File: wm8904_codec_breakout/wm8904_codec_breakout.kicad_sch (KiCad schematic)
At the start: 5 parts, among them J101 Conn_01x12_Female, J102 Conn_01x12_Female, J103 AudioJack3, J104 AudioJack3, U101 AMS1117-1.8

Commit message: WIP
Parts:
- added TP101: 1V8, TestPoint:TestPoint_Pad_D1.5mm, symbol Connector:TestPoint
- added TP102: GND, TestPoint:TestPoint_Pad_D1.5mm, symbol Connector:TestPoint
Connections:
- net 1V8: now also TP101.1
- net GND: now also TP102.1
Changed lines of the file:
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@@
+    )
+  )
+  (global_label "1V8" (shape input) (at 205.74 52.07 270) (fields_autoplaced)
+    (effects (font (size 1.27 1.27)) (justify right))
+    (property "Intersheet References" "${INTERSHEET_REFS}" (id 0) (at 205.8194 57.9907 90)
+      (effects (font (size 1.27 1.27)) (justify right) hide)
     )
   )
@@
     (pin "T")
   )
+  (symbol (lib_id "power:GND") (at 205.74 35.56 0) (unit 1)
+    (in_bom yes) (on_board yes) (fields_autoplaced)
+    (property "Reference" "#PWR0123" (id 0) (at 205.74 41.91 0)
+      (effects (font (size 1.27 1.27)) hide)
+    )
+    (property "Value" "GND" (id 1) (at 205.74 40.64 0))
+    (property "Footprint" "" (id 2) (at 205.74 35.56 0)
+      (effects (font (size 1.27 1.27)) hide)
+    )
+    (property "Datasheet" "" (id 3) (at 205.74 35.56 0)
+      (effects (font (size 1.27 1.27)) hide)
+    )
+    (pin "1")
+  )
   (symbol (lib_id "Connector:Conn_01x12_Female") (at 121.92 83.82 0) (unit 1)
     (in_bom yes) (on_board yes) (fields_autoplaced)
@@
     (pin "1")
   )
+  (symbol (lib_id "Connector:TestPoint") (at 205.74 52.07 0) (unit 1)
+    (in_bom yes) (on_board yes) (fields_autoplaced)
+    (property "Reference" "TP101" (id 0) (at 208.28 47.4979 0)
+      (effects (font (size 1.27 1.27)) (justify left))
+    )
+    (property "Value" "1V8" (id 1) (at 208.28 50.0379 0)
+      (effects (font (size 1.27 1.27)) (justify left))
+    )
+    (property "Footprint" "TestPoint:TestPoint_Pad_D1.5mm" (id 2) (at 210.82 52.07 0))
+    (property "Datasheet" "~" (id 3) (at 210.82 52.07 0)
+      (effects (font (size 1.27 1.27)) hide)
+    )
+    (property "JLCPCB BOM" "False" (id 4) (at 205.74 52.07 0)
+      (effects (font (size 1.27 1.27)) hide)
+    )
+    (pin "1")
+  )
   (symbol (lib_id "power:GND") (at 114.3 138.43 0) (unit 1)
     (in_bom yes) (on_board yes) (fields_autoplaced)
@@
     (pin "2")
     (pin "3")
+  )
+  (symbol (lib_id "Connector:TestPoint") (at 205.74 35.56 0) (unit 1)
+    (in_bom yes) (on_board yes) (fields_autoplaced)
+    (property "Reference" "TP102" (id 0) (at 208.28 30.9879 0)
+      (effects (font (size 1.27 1.27)) (justify left))
+    )
+    (property "Value" "GND" (id 1) (at 208.28 33.5279 0)
+      (effects (font (size 1.27 1.27)) (justify left))
+    )
+    (property "Footprint" "TestPoint:TestPoint_Pad_D1.5mm" (id 2) (at 210.82 35.56 0))
+    (property "Datasheet" "~" (id 3) (at 210.82 35.56 0)
+      (effects (font (size 1.27 1.27)) hide)
+    )
+    (property "JLCPCB BOM" "False" (id 4) (at 205.74 35.56 0)
+      (effects (font (size 1.27 1.27)) hide)
+    )
+    (pin "1")
   )
   (sheet (at 180.34 69.85) (size 30.48 74.93) (fields_autoplaced)
@@
       (reference "#PWR0122") (unit 1) (value "GND") (footprint "")
     )
+    (path "/43064d00-084c-4e4c-8e6c-67264db5fdd4"
+      (reference "#PWR0123") (unit 1) (value "GND") (footprint "")
+    )
     (path "/7803a0ea-b6d3-457b-b195-42c8dc80b579/b0748b99-67ee-4e5a-be57-fcef590b69aa"
       (reference "C201") (unit 1) (value "0.1u") (footprint "Capacitor_SMD:C_0402_1005Metric")
@@
       (reference "R206") (unit 1) (value "20R") (footprint "Resistor_SMD:R_0603_1608Metric")
     )
+    (path "/6f172490-e7c3-45a0-aafa-f94d5c12df3c"
+      (reference "TP101") (unit 1) (value "1V8") (footprint "TestPoint:TestPoint_Pad_D1.5mm")
+    )
+    (path "/ae81fe48-d57e-4488-a23e-f57c11561913"
+      (reference "TP102") (unit 1) (value "GND") (footprint "TestPoint:TestPoint_Pad_D1.5mm")
+    )
     (path "/952e9d28-22f9-43e0-bee5-7380cf9b61ad"

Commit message: final touches + v1 jlcpcb fab files
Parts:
- removed TP101: 1V8, TestPoint:TestPoint_Pad_D1.5mm, symbol Connector:TestPoint
- removed TP102: GND, TestPoint:TestPoint_Pad_D1.5mm, symbol Connector:TestPoint
- J103, J104: LCSC Part (none) -> C707224; MSCS Part C707224 -> (none)
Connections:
- net 1V8: now also J101.12 (Pin_12)
- net VDD: no longer J101.12 (Pin_12)
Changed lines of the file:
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@@
-    )
-  )
-  (global_label "VDD" (shape input) (at 116.84 99.06 180) (fields_autoplaced)
-    (effects (font (size 1.27 1.27)) (justify right))
-    (property "Intersheet References" "${INTERSHEET_REFS}" (id 0) (at 110.7983 98.9806 0)
-      (effects (font (size 1.27 1.27)) (justify right) hide)
     )
   )
@@
     )
   )
-  (global_label "1V8" (shape input) (at 205.74 52.07 270) (fields_autoplaced)
-    (effects (font (size 1.27 1.27)) (justify right))
-    (property "Intersheet References" "${INTERSHEET_REFS}" (id 0) (at 205.8194 57.9907 90)
-      (effects (font (size 1.27 1.27)) (justify right) hide)
-    )
-  )
   (global_label "LINEOUTFB" (shape input) (at 180.34 87.63 180) (fields_autoplaced)
     (effects (font (size 1.27 1.27)) (justify right))
@@
     (effects (font (size 1.27 1.27)) (justify right))
     (property "Intersheet References" "${INTERSHEET_REFS}" (id 0) (at 107.4721 91.3606 0)
+      (effects (font (size 1.27 1.27)) (justify right) hide)
+    )
+  )
+  (global_label "1V8" (shape input) (at 116.84 99.06 180) (fields_autoplaced)
+    (effects (font (size 1.27 1.27)) (justify right))
+    (property "Intersheet References" "${INTERSHEET_REFS}" (id 0) (at 110.9193 99.1394 0)
       (effects (font (size 1.27 1.27)) (justify right) hide)
     )
@@
       (effects (font (size 1.27 1.27)) hide)
     )
-    (property "MSCS Part" "C707224" (id 4) (at 177.8 53.34 0)
+    (property "LCSC Part" "C707224" (id 4) (at 177.8 53.34 0)
       (effects (font (size 1.27 1.27)) hide)
     )
@@
       (effects (font (size 1.27 1.27)) hide)
     )
-    (property "MSCS Part" "C707224" (id 4) (at 177.8 35.56 0)
+    (property "LCSC Part" "C707224" (id 4) (at 177.8 35.56 0)
       (effects (font (size 1.27 1.27)) hide)
     )
@@
     (pin "S")
     (pin "T")
-  )
-  (symbol (lib_id "power:GND") (at 205.74 35.56 0) (unit 1)
-    (in_bom yes) (on_board yes) (fields_autoplaced)
-    (property "Reference" "#PWR0123" (id 0) (at 205.74 41.91 0)
-      (effects (font (size 1.27 1.27)) hide)
-    )
-    (property "Value" "GND" (id 1) (at 205.74 40.64 0))
-    (property "Footprint" "" (id 2) (at 205.74 35.56 0)
-      (effects (font (size 1.27 1.27)) hide)
-    )
-    (property "Datasheet" "" (id 3) (at 205.74 35.56 0)
-      (effects (font (size 1.27 1.27)) hide)
-    )
-    (pin "1")
   )
   (symbol (lib_id "Connector:Conn_01x12_Female") (at 121.92 83.82 0) (unit 1)
@@
     (pin "1")
   )
-  (symbol (lib_id "Connector:TestPoint") (at 205.74 52.07 0) (unit 1)
-    (in_bom yes) (on_board yes) (fields_autoplaced)
-    (property "Reference" "TP101" (id 0) (at 208.28 47.4979 0)
-      (effects (font (size 1.27 1.27)) (justify left))
-    )
-    (property "Value" "1V8" (id 1) (at 208.28 50.0379 0)
-      (effects (font (size 1.27 1.27)) (justify left))
-    )
-    (property "Footprint" "TestPoint:TestPoint_Pad_D1.5mm" (id 2) (at 210.82 52.07 0))
-    (property "Datasheet" "~" (id 3) (at 210.82 52.07 0)
-      (effects (font (size 1.27 1.27)) hide)
-    )
-    (property "JLCPCB BOM" "False" (id 4) (at 205.74 52.07 0)
-      (effects (font (size 1.27 1.27)) hide)
-    )
-    (pin "1")
-  )
   (symbol (lib_id "power:GND") (at 114.3 138.43 0) (unit 1)
     (in_bom yes) (on_board yes) (fields_autoplaced)
@@
     (pin "2")
     (pin "3")
-  )
-  (symbol (lib_id "Connector:TestPoint") (at 205.74 35.56 0) (unit 1)
-    (in_bom yes) (on_board yes) (fields_autoplaced)
-    (property "Reference" "TP102" (id 0) (at 208.28 30.9879 0)
-      (effects (font (size 1.27 1.27)) (justify left))
-    )
-    (property "Value" "GND" (id 1) (at 208.28 33.5279 0)
-      (effects (font (size 1.27 1.27)) (justify left))
-    )
-    (property "Footprint" "TestPoint:TestPoint_Pad_D1.5mm" (id 2) (at 210.82 35.56 0))
-    (property "Datasheet" "~" (id 3) (at 210.82 35.56 0)
-      (effects (font (size 1.27 1.27)) hide)
-    )
-    (property "JLCPCB BOM" "False" (id 4) (at 205.74 35.56 0)
-      (effects (font (size 1.27 1.27)) hide)
-    )
-    (pin "1")
   )
   (sheet (at 180.34 69.85) (size 30.48 74.93) (fields_autoplaced)
@@
       (reference "#PWR0122") (unit 1) (value "GND") (footprint "")
     )
-    (path "/43064d00-084c-4e4c-8e6c-67264db5fdd4"
-      (reference "#PWR0123") (unit 1) (value "GND") (footprint "")
-    )
     (path "/7803a0ea-b6d3-457b-b195-42c8dc80b579/b0748b99-67ee-4e5a-be57-fcef590b69aa"
       (reference "C201") (unit 1) (value "0.1u") (footprint "Capacitor_SMD:C_0402_1005Metric")
@@
       (reference "R206") (unit 1) (value "20R") (footprint "Resistor_SMD:R_0603_1608Metric")
     )
-    (path "/6f172490-e7c3-45a0-aafa-f94d5c12df3c"
-      (reference "TP101") (unit 1) (value "1V8") (footprint "TestPoint:TestPoint_Pad_D1.5mm")
-    )
-    (path "/ae81fe48-d57e-4488-a23e-f57c11561913"
-      (reference "TP102") (unit 1) (value "GND") (footprint "TestPoint:TestPoint_Pad_D1.5mm")
-    )
     (path "/952e9d28-22f9-43e0-bee5-7380cf9b61ad"

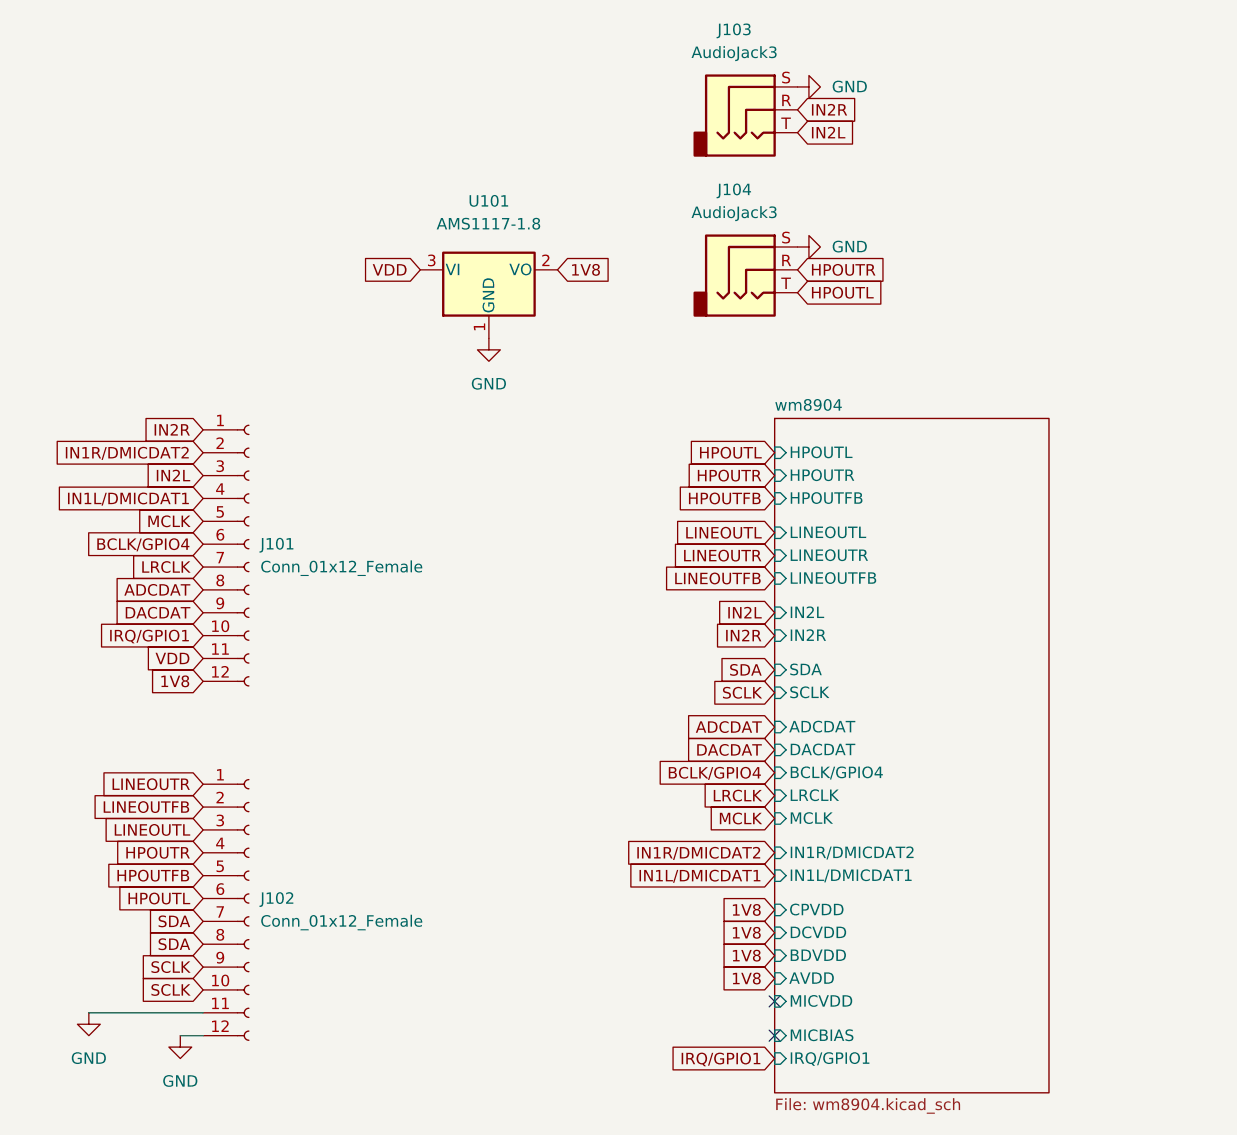
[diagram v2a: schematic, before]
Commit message: [wm8904_codec_breakout] connect LINEOUTFB and HPOUTFB to ground and bump board version to v2
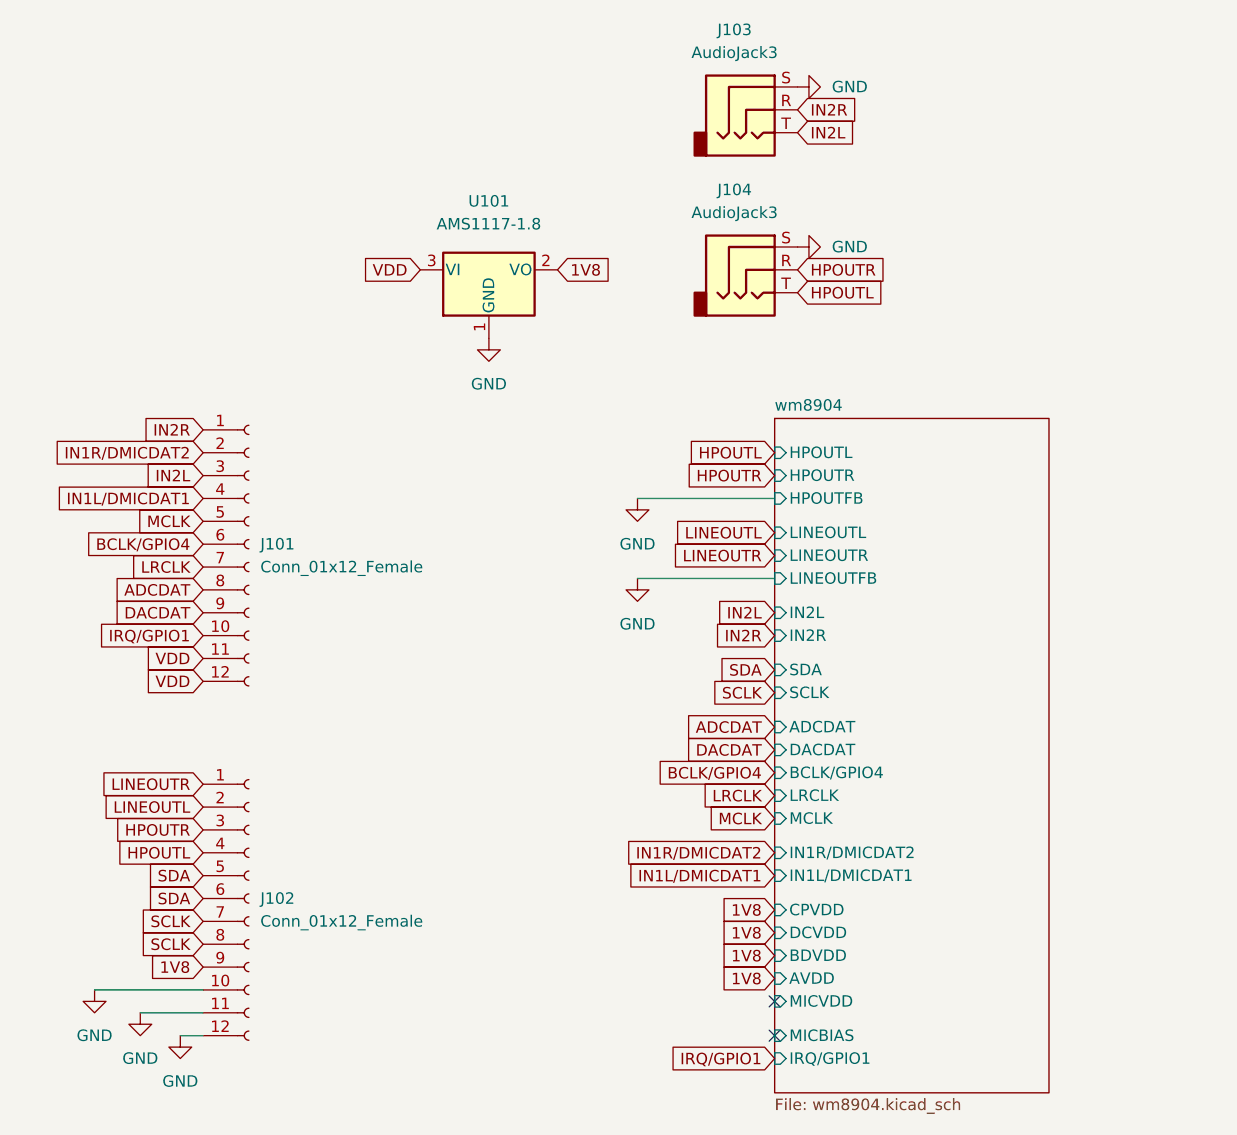
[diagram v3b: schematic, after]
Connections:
- net HPOUTFB is gone; now on net SDA: J102.5 (Pin_5)
- net LINEOUTFB is gone; now on net LINEOUTL: J102.2 (Pin_2)
- net 1V8: now also J102.9 (Pin_9); no longer J101.12 (Pin_12)
- net GND: now also J102.10 (Pin_10)
- net HPOUTL: now also J102.4 (Pin_4); no longer J102.6 (Pin_6)
- net HPOUTR: now also J102.3 (Pin_3); no longer J102.4 (Pin_4)
- net LINEOUTL: no longer J102.3 (Pin_3)
- net SCLK: now also J102.7 (Pin_7), J102.8 (Pin_8); no longer J102.10 (Pin_10), J102.9 (Pin_9)
- net SDA: now also J102.6 (Pin_6); no longer J102.7 (Pin_7), J102.8 (Pin_8)
- net VDD: now also J101.12 (Pin_12)
